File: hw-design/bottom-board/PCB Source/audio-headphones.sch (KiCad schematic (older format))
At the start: 26 parts, among them Q17 J110, Q8 J110, U14 LM4811

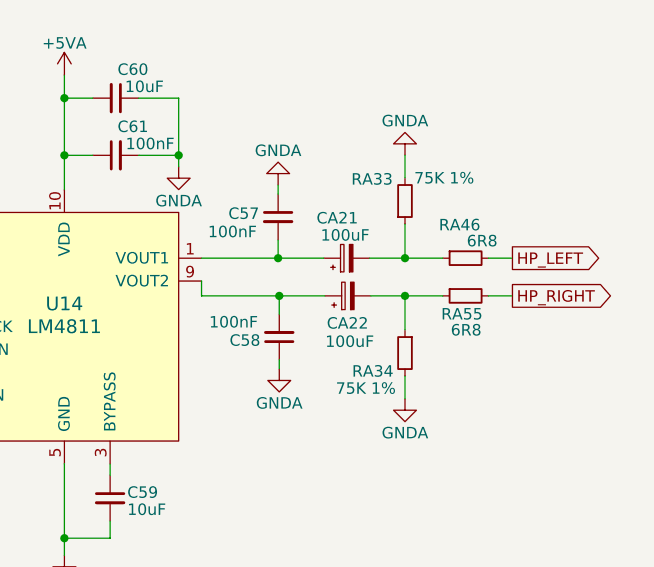
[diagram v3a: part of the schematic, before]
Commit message: update all MPN's to match the Dwarf
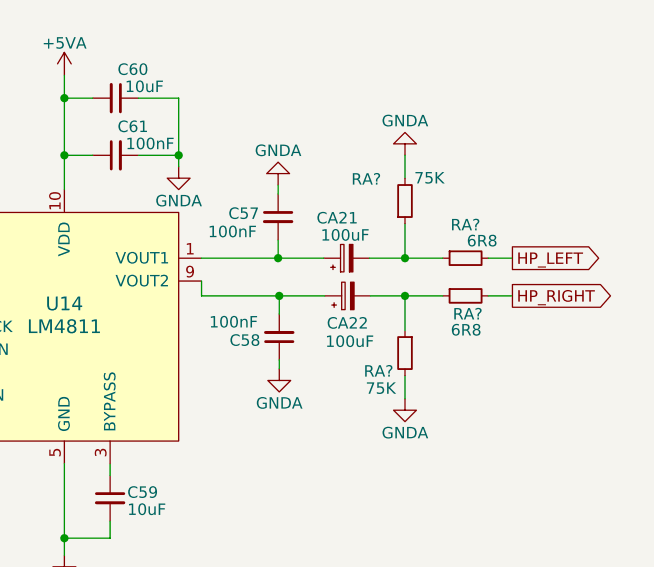
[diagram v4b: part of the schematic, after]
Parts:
- C59, C60: footprint Capacitor_SMD:C_0603_1608Metric -> Capacitor_SMD:C_0805_2012Metric; MPN CL10A106MQ8NNNC -> GRM219R61E106KA12D
- CA21, CA22: MPN UWX1C101MCL1GB -> 107SML016M
- R71, R72: MPN RMCF0603FT56K0 -> RT0603DRD0756KL
- R?: renamed from RA33; value 75K 1% -> 75K
- R?: renamed from RA34; value 75K 1% -> 75K
- R?: renamed from RA46; MPN (none) -> RMCF0603FT6R80
- R?: renamed from RA55; MPN (none) -> RMCF0603FT6R80
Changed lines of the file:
@@
 Sheet 7 13
 Title "MOD DuoX - Bottom Board"
-Date "2020-05-15"
-Rev "Rev 1.12"
+Date "2021-11-11"
+Rev "Rev 1.05"
 Comp "MOD Devices GmbH"
 Comment1 "DuoX Audio processing board"
 Comment2 "https://github.com/moddevices/mod-hw-duoX"
-Comment3 ""
-Comment4 ""
+Comment3 "Inp Power: 12V 700mA"
+Comment4 "USB outp Power: 500mA"
 $EndDescr
 $Comp
@@
 F 0 "C59" H 6275 3825 50  0000 R CNN
 F 1 "10uF" H 6275 3750 50  0000 R CNN
-F 2 "Capacitor_SMD:C_0603_1608Metric" H 6350 3800 60  0001 C CNN
+F 2 "Capacitor_SMD:C_0805_2012Metric" H 6350 3800 60  0001 C CNN
 F 3 "" H 6350 3800 60  0000 C CNN
-F 4 "CL10A106MQ8NNNC" H 1050 -1550 50  0001 C CNN "MPN"
+F 4 "GRM219R61E106KA12D" H 1050 -1550 50  0001 C CNN "MPN"
 	1    6350 3800
 	-1   0    0    -1
@@
 F 0 "C60" V 6500 2125 50  0000 C CNN
 F 1 "10uF" V 6425 2175 50  0000 C CNN
-F 2 "Capacitor_SMD:C_0603_1608Metric" H 6375 2050 60  0001 C CNN
+F 2 "Capacitor_SMD:C_0805_2012Metric" H 6375 2050 60  0001 C CNN
 F 3 "" H 6375 2050 60  0000 C CNN
-F 4 "CL10A106MQ8NNNC" H 1075 -3300 50  0001 C CNN "MPN"
+F 4 "GRM219R61E106KA12D" H 1075 -3300 50  0001 C CNN "MPN"
 	1    6375 2050
 	0    1    -1   0
@@
 F 2 "Capacitor_SMD:CP_Elec_6.3x7.7" H 7385 2750 60  0001 C CNN
 F 3 "" H 7385 2750 60  0000 C CNN
-F 4 "UWX1C101MCL1GB" H 2035 1100 50  0001 C CNN "MPN"
+F 4 "107SML016M" H 2035 1100 50  0001 C CNN "MPN"
 	1    7385 2750
 	0    -1   -1   0
@@
 F 2 "Capacitor_SMD:CP_Elec_6.3x7.7" H 7390 2915 60  0001 C CNN
 F 3 "" H 7390 2915 60  0000 C CNN
-F 4 "UWX1C101MCL1GB" H 2040 1265 50  0001 C CNN "MPN"
+F 4 "107SML016M" H 2040 1265 50  0001 C CNN "MPN"
 	1    7390 2915
 	0    -1   -1   0
@@
 P 7640 2500
 AR Path="/54F72CD0/5B6B7B84" Ref="RA?"  Part="1"
-AR Path="/54F72F64/5B6B7B84" Ref="RA33"  Part="1"
-F 0 "RA33" H 7405 2405 50  0000 L CNN
-F 1 "75K 1%" H 7680 2400 50  0000 L CNN
+AR Path="/54F72F64/5B6B7B84" Ref="R?"  Part="1"
+F 0 "R?" H 7405 2405 50  0000 L CNN
+F 1 "75K" H 7680 2400 50  0000 L CNN
 F 2 "Resistor_SMD:R_0603_1608Metric" H 7640 2500 60  0001 C CNN
 F 3 "" H 7640 2500 60  0000 C CNN
@@
 P 7640 3165
 AR Path="/54F72CD0/5B6BCC20" Ref="RA?"  Part="1"
-AR Path="/54F72F64/5B6BCC20" Ref="RA34"  Part="1"
-F 0 "RA34" H 7690 3085 50  0000 L CNN
-F 1 "75K 1%" H 7680 3010 50  0000 L CNN
+AR Path="/54F72F64/5B6BCC20" Ref="R?"  Part="1"
+F 0 "R?" H 7690 3085 50  0000 L CNN
+F 1 "75K" H 7680 3010 50  0000 L CNN
 F 2 "Resistor_SMD:R_0603_1608Metric" H 7640 3165 60  0001 C CNN
 F 3 "" H 7640 3165 60  0000 C CNN
@@
 F 2 "Resistor_SMD:R_0603_1608Metric" H 3250 3800 60  0001 C CNN
 F 3 "" H 3250 3800 60  0000 C CNN
-F 4 "RMCF0603FT56K0" H -1050 1450 50  0001 C CNN "MPN"
+F 4 "RT0603DRD0756KL" H -1050 1450 50  0001 C CNN "MPN"
 	1    3250 3800
 	-1   0    0    1
@@
 F 2 "Resistor_SMD:R_0603_1608Metric" H 3250 2350 60  0001 C CNN
 F 3 "" H 3250 2350 60  0000 C CNN
-F 4 "RMCF0603FT56K0" H -1050 0   50  0001 C CNN "MPN"
+F 4 "RT0603DRD0756KL" H -1050 0   50  0001 C CNN "MPN"
 	1    3250 2350
 	-1   0    0    1
@@
 P 7905 2750
 AR Path="/54F72CD0/62578939" Ref="RA?"  Part="1"
-AR Path="/54F72F64/62578939" Ref="RA46"  Part="1"
-F 0 "RA46" V 7760 2685 50  0000 L CNN
+AR Path="/54F72F64/62578939" Ref="R?"  Part="1"
+F 0 "R?" V 7760 2685 50  0000 L CNN
 F 1 "6R8" V 7830 2610 50  0000 L CNN
 F 2 "Resistor_SMD:R_0603_1608Metric" H 7905 2750 60  0001 C CNN
 F 3 "" H 7905 2750 60  0000 C CNN
-F 4 "" H 3855 350 50  0001 C CNN "MPN"
+F 4 "RMCF0603FT6R80" H 3855 350 50  0001 C CNN "MPN"
 	1    7905 2750
 	0    -1   1    0
@@
 P 7905 2915
 AR Path="/54F72CD0/62598A2E" Ref="RA?"  Part="1"
-AR Path="/54F72F64/62598A2E" Ref="RA55"  Part="1"
-F 0 "RA55" V 7985 2840 50  0000 L CNN
+AR Path="/54F72F64/62598A2E" Ref="R?"  Part="1"
+F 0 "R?" V 7985 2840 50  0000 L CNN
 F 1 "6R8" V 8055 2845 50  0000 L CNN
 F 2 "Resistor_SMD:R_0603_1608Metric" H 7905 2915 60  0001 C CNN
 F 3 "" H 7905 2915 60  0000 C CNN
-F 4 "" H 3855 515 50  0001 C CNN "MPN"
+F 4 "RMCF0603FT6R80" H 3855 515 50  0001 C CNN "MPN"
 	1    7905 2915
 	0    -1   1    0

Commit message: update fabrication files
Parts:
- gave numbers to parts that had none: 4
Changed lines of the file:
@@
 P 7640 2500
 AR Path="/54F72CD0/5B6B7B84" Ref="RA?"  Part="1"
-AR Path="/54F72F64/5B6B7B84" Ref="R?"  Part="1"
-F 0 "R?" H 7405 2405 50  0000 L CNN
+AR Path="/54F72F64/5B6B7B84" Ref="R129"  Part="1"
+F 0 "R129" H 7405 2405 50  0000 L CNN
 F 1 "75K" H 7680 2400 50  0000 L CNN
 F 2 "Resistor_SMD:R_0603_1608Metric" H 7640 2500 60  0001 C CNN
@@
 P 7640 3165
 AR Path="/54F72CD0/5B6BCC20" Ref="RA?"  Part="1"
-AR Path="/54F72F64/5B6BCC20" Ref="R?"  Part="1"
-F 0 "R?" H 7690 3085 50  0000 L CNN
+AR Path="/54F72F64/5B6BCC20" Ref="R130"  Part="1"
+F 0 "R130" H 7690 3085 50  0000 L CNN
 F 1 "75K" H 7680 3010 50  0000 L CNN
 F 2 "Resistor_SMD:R_0603_1608Metric" H 7640 3165 60  0001 C CNN
@@
 P 7905 2750
 AR Path="/54F72CD0/62578939" Ref="RA?"  Part="1"
-AR Path="/54F72F64/62578939" Ref="R?"  Part="1"
-F 0 "R?" V 7760 2685 50  0000 L CNN
+AR Path="/54F72F64/62578939" Ref="R131"  Part="1"
+F 0 "R131" V 7760 2685 50  0000 L CNN
 F 1 "6R8" V 7830 2610 50  0000 L CNN
 F 2 "Resistor_SMD:R_0603_1608Metric" H 7905 2750 60  0001 C CNN
@@
 P 7905 2915
 AR Path="/54F72CD0/62598A2E" Ref="RA?"  Part="1"
-AR Path="/54F72F64/62598A2E" Ref="R?"  Part="1"
-F 0 "R?" V 7985 2840 50  0000 L CNN
+AR Path="/54F72F64/62598A2E" Ref="R132"  Part="1"
+F 0 "R132" V 7985 2840 50  0000 L CNN
 F 1 "6R8" V 8055 2845 50  0000 L CNN
 F 2 "Resistor_SMD:R_0603_1608Metric" H 7905 2915 60  0001 C CNN
